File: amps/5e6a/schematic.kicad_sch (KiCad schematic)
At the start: 62 parts, among them T3 part not legible

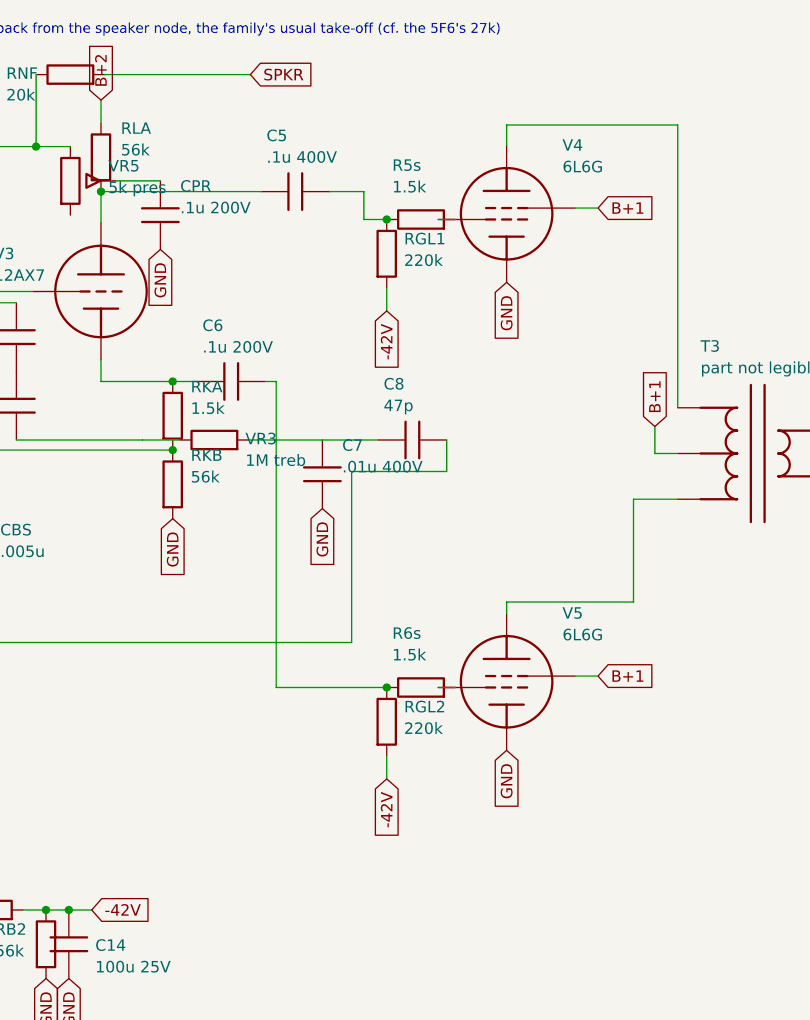
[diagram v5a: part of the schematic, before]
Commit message: Fix: schematic wiring on 5c1, 5e1, 5e4a, 5e5a, 5e6a, 5f4; all six claim equivalence
- 5c1, 5e1: the B+1/B+2/B+3 labels sat 3.56 mm above the filter chain with
  no lead, naming rails the drawing never reached
- 5e4a, 5e5a, 5e6a, 5f4: the 220k grid leak tapped the coupling-cap node;
  the netlist and the factory-derived layouts both return it at the grid
  pin after the 1.5k stopper (coupler -> stopper -> grid, as jtm45 draws
  it); each stopper now lands on the pentode's own grid pin and the leak
  hangs off that junction
- sch_map.yaml schematic_claim: verified on all six -> 37 of 38 sheets are
  hard-gated; 6g5 stays unclaimed (presence-branch DC path is a source
  question, not a declaration)

Co-Authored-By: Claude Fable 5.1 <noreply@anthropic.com>
Claude-Session: https://claude.ai/code/session_01KBMfdh37HmCL2iWcBiL5J1
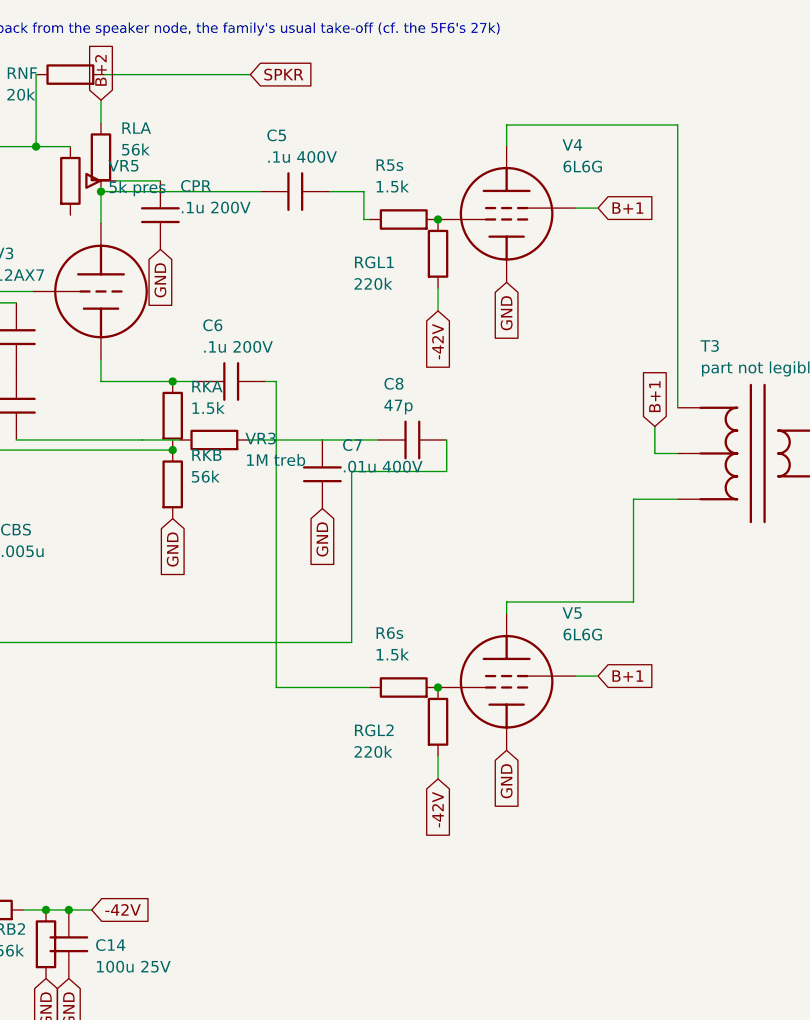
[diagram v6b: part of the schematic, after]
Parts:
- removed RB1: 3.3k, symbol cx:R
- removed RD2: 10k, symbol cx:R
- added C12: 16u, symbol cx:C
- added D1: SEL, symbol cx:DIODE_SS
- RB1: renamed from D1; value SEL -> 3.3k; symbol cx:DIODE_SS -> cx:R
- RD2: renamed from C12; value 16u -> 10k; symbol cx:C -> cx:R
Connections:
- net -42V: now also RB1.2
- net B+2: now also C12.1
- net B+3: now also RD2.2
- net GND: now also C12.2; no longer RD2.2
- net HT_B: now also D1.1 (A); no longer RB1.1 (A)
- net at R5s.2, V4.2 (G1): now also RGL1.1
- net at C5.2, R5s.1: no longer RGL1.1
- net at C6.2, R6s.1: no longer RGL2.1
- net at R6s.2, V5.2 (G1): now also RGL2.1
- new net: D1.2 (K), RB1.1
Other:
- moved on the sheet: R5s
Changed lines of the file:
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@@
   (wire (pts (xy 205.242 31.37) (xy 205.242 34.47))
     (stroke (width 0) (type default)))
-  (wire (pts (xy 205.242 34.47) (xy 207.782 34.47))
-    (stroke (width 0) (type default)))
-  (symbol (lib_id "cx:R") (at 211.592 34.47 90) (unit 1)
-    (in_bom yes) (on_board yes)
-    (property "Reference" "R5s" (at 208.392 28.47 270) (effects (font (size 1.27 1.27)) (justify left)))
-    (property "Value" "1.5k" (at 208.392 30.87 270) (effects (font (size 1.27 1.27)) (justify left))))
   (symbol (lib_id "cx:PENTODE") (at 221.102 33.835 0) (unit 1)
     (in_bom yes) (on_board yes)
     (property "Reference" "V4" (at 227.302 26.235 0) (effects (font (size 1.27 1.27)) (justify left)))
     (property "Value" "6L6G" (at 227.302 28.635 0) (effects (font (size 1.27 1.27)) (justify left))))
-  (wire (pts (xy 215.402 34.47) (xy 213.482 34.47))
+  (symbol (lib_id "cx:R") (at 209.672 34.47 90) (unit 1)
+    (in_bom yes) (on_board yes)
+    (property "Reference" "R5s" (at 206.472 28.47 270) (effects (font (size 1.27 1.27)) (justify left)))
+    (property "Value" "1.5k" (at 206.472 30.87 270) (effects (font (size 1.27 1.27)) (justify left))))
+  (wire (pts (xy 205.242 34.47) (xy 205.862 34.47))
     (stroke (width 0) (type default)))
-  (junction (at 207.782 34.47) (diameter 0) (color 0 0 0 0))
-  (symbol (lib_id "cx:R") (at 207.782 38.28 0) (unit 1)
+  (junction (at 213.482 34.47) (diameter 0) (color 0 0 0 0))
+  (symbol (lib_id "cx:R") (at 213.482 38.28 0) (unit 1)
     (in_bom yes) (on_board yes)
-    (property "Reference" "RGL1" (at 209.698 36.64 0) (effects (font (size 1.27 1.27)) (justify left)))
-    (property "Value" "220k" (at 209.698 39.04 0) (effects (font (size 1.27 1.27)) (justify left))))
-  (wire (pts (xy 207.782 42.09) (xy 207.782 44.63))
+    (property "Reference" "RGL1" (at 204.082 39.28 0) (effects (font (size 1.27 1.27)) (justify left)))
+    (property "Value" "220k" (at 204.082 41.68 0) (effects (font (size 1.27 1.27)) (justify left))))
+  (wire (pts (xy 213.482 42.09) (xy 213.482 44.63))
     (stroke (width 0) (type default)))
-  (global_label "-42V" (shape input) (at 207.782 44.63 270)
+  (global_label "-42V" (shape input) (at 213.482 44.63 270)
     (effects (font (size 1.27 1.27)) (justify right)))
   (wire (pts (xy 228.722 33.2) (xy 231.262 33.2))
@@
   (wire (pts (xy 195.502 86.47) (xy 205.242 86.47))
     (stroke (width 0) (type default)))
-  (wire (pts (xy 205.242 86.47) (xy 207.782 86.47))
-    (stroke (width 0) (type default)))
-  (symbol (lib_id "cx:R") (at 211.592 86.47 90) (unit 1)
-    (in_bom yes) (on_board yes)
-    (property "Reference" "R6s" (at 208.392 80.47 270) (effects (font (size 1.27 1.27)) (justify left)))
-    (property "Value" "1.5k" (at 208.392 82.87 270) (effects (font (size 1.27 1.27)) (justify left))))
   (symbol (lib_id "cx:PENTODE") (at 221.102 85.835 0) (unit 1)
     (in_bom yes) (on_board yes)
     (property "Reference" "V5" (at 227.302 78.235 0) (effects (font (size 1.27 1.27)) (justify left)))
     (property "Value" "6L6G" (at 227.302 80.635 0) (effects (font (size 1.27 1.27)) (justify left))))
-  (wire (pts (xy 215.402 86.47) (xy 213.482 86.47))
+  (symbol (lib_id "cx:R") (at 209.672 86.47 90) (unit 1)
+    (in_bom yes) (on_board yes)
+    (property "Reference" "R6s" (at 206.472 80.47 270) (effects (font (size 1.27 1.27)) (justify left)))
+    (property "Value" "1.5k" (at 206.472 82.87 270) (effects (font (size 1.27 1.27)) (justify left))))
+  (wire (pts (xy 205.242 86.47) (xy 205.862 86.47))
     (stroke (width 0) (type default)))
-  (junction (at 207.782 86.47) (diameter 0) (color 0 0 0 0))
-  (symbol (lib_id "cx:R") (at 207.782 90.28 0) (unit 1)
+  (junction (at 213.482 86.47) (diameter 0) (color 0 0 0 0))
+  (symbol (lib_id "cx:R") (at 213.482 90.28 0) (unit 1)
     (in_bom yes) (on_board yes)
-    (property "Reference" "RGL2" (at 209.698 88.64 0) (effects (font (size 1.27 1.27)) (justify left)))
-    (property "Value" "220k" (at 209.698 91.04 0) (effects (font (size 1.27 1.27)) (justify left))))
-  (wire (pts (xy 207.782 94.09) (xy 207.782 96.63))
+    (property "Reference" "RGL2" (at 204.082 91.28 0) (effects (font (size 1.27 1.27)) (justify left)))
+    (property "Value" "220k" (at 204.082 93.68 0) (effects (font (size 1.27 1.27)) (justify left))))
+  (wire (pts (xy 213.482 94.09) (xy 213.482 96.63))
     (stroke (width 0) (type default)))
-  (global_label "-42V" (shape input) (at 207.782 96.63 270)
+  (global_label "-42V" (shape input) (at 213.482 96.63 270)
     (effects (font (size 1.27 1.27)) (justify right)))
   (wire (pts (xy 228.722 85.2) (xy 231.262 85.2))

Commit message: Add: real tube pin numbers and readable valve glyphs on every schematic
Phase B of the drawing program. A factory service sheet numbers every tube
pin, because the number is what a technician puts a probe on. This corpus
printed none, and the numbers hidden in its symbols were positional
placeholders (P=1, G=2, K=3) that would have published a 6V6GT's plate as
pin 1 when it is pin 3.

1055 electrodes now carry the real number, 1027 lettered (27 are shared
filaments deduped, 1 dropped for want of clear space on the 6G2). Resolved per
instance from reference/tubes/<slug>.yaml through the same alias resolution the
layout renderer uses, so a 12AX7 section and a 6SL7 section each get their own
basing. A valve whose basing the corpus does not carry prints nothing rather
than a wrong number.

Section letters and basing units are now separate things, which cost a detour
worth recording. The RCA 12AX7-A sheet reads "Pin 1 - Plate of Unit No.2 ...
Pin 6 - Plate of Unit No.1", so unit numbering is not pin order; the 5Y3 and
GZ34 number their units in opposite pin order, so nothing positional can
express it. But the section LETTER is a designator, not a basing fact: this
corpus, like every technician, calls the first stage in signal order V1A, and
five amps' prose already did. On four amps the factory sheets put that first
stage on the other half -- the AA764's own schematic prints +200 V on pin 1 --
so those drawings now state their unit explicitly, each citing its source, and
no letter, netlist, parts list or layout comment changed. 183 layout comments
agree with the printed numbers, 0 disagree. A guard fires if two halves of one
bottle resolve to the same unit, which is exactly how this was found.

Glyphs: the cathode gains a bracket and filament hairpin so it can no longer be
confused with the plate bar, the pentode's screen sits on its own row, and a
rectifier draws as one envelope over its sections instead of two apparent
bottles. Line weights are scaled per sheet to a co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
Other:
- note added: "1"
- note added: "2"
- note added: "2,8"
- note added: "3"
- note added: "4"
- note added: "5"
- note added: "6"
- note added: "7"
- note added: "8"

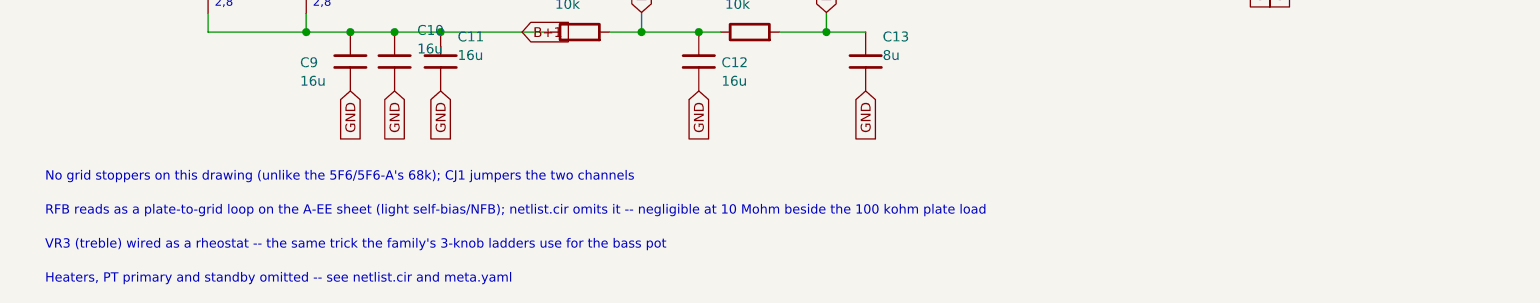
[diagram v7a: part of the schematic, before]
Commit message: Fix: schematic sheet notes no longer name repository files
Thirty-seven committed sheets rendered footnotes and section notes such as
"Heaters and PT primary omitted — see netlist.cir and meta.yaml" or
"excluded from netlist.cir (notes.md)" to visitors through KiCanvas. The
prose sweeps never counted sheets. Rewritten in the site's own words — the
netlist, the sources list, the circuit story, the parts list, the board
drawing — in 59 strings across 33 draw scripts, keeping every technical
claim as it was; the three tone sheets (6G4, 6G5, 6G6-B) are under repair
elsewhere and keep theirs for now. The sweep touched only strings passed to
the sheet's note, text, caption and footnote calls, never a path or a value.

Gates: check_schematics 40/0, connectivity 0 isolated pins;
verify_schematic_nets 40 clean; only the regenerated sheets and their served
copies changed.

Co-Authored-By: Claude Fable 5.1 <noreply@anthropic.com>
Claude-Session: https://claude.ai/code/session_01KBMfdh37HmCL2iWcBiL5J1
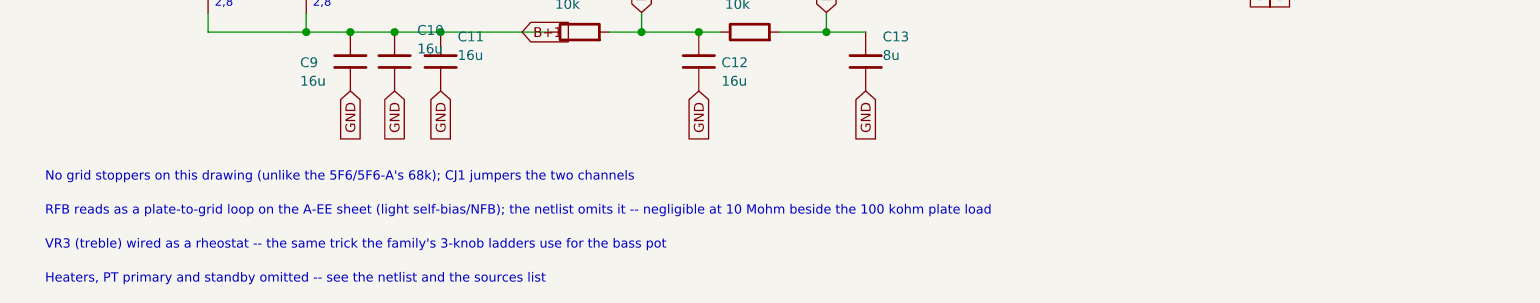
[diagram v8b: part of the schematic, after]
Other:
- note added: "Heaters, PT primary and standby omitted -- see the netlist and the sources list"
- note added: "RFB reads as a plate-to-grid loop on the A-EE sheet (light self-bias/NFB); the netlist omits it -- negligible at 10 Mohm beside the 100 kohm plate load"
- note removed: "Heaters, PT primary and standby omitted -- see netlist.cir and meta.yaml"
- note removed: "RFB reads as a plate-to-grid loop on the A-EE sheet (light self-bias/NFB); netlist.cir omits it -- negligible at 10 Mohm beside the 100 kohm plate load"
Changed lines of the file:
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@@
   (text "No grid stoppers on this drawing (unlike the 5F6/5F6-A's 68k); CJ1 jumpers the two channels" (at 12.7 147.048 0)
     (effects (font (size 1.2 1.2)) (justify left)))
-  (text "RFB reads as a plate-to-grid loop on the A-EE sheet (light self-bias/NFB); netlist.cir omits it -- negligible at 10 Mohm beside the 100 kohm plate load" (at 12.7 151.448 0)
+  (text "RFB reads as a plate-to-grid loop on the A-EE sheet (light self-bias/NFB); the netlist omits it -- negligible at 10 Mohm beside the 100 kohm plate load" (at 12.7 151.448 0)
     (effects (font (size 1.2 1.2)) (justify left)))
   (text "VR3 (treble) wired as a rheostat -- the same trick the family's 3-knob ladders use for the bass pot" (at 12.7 155.848 0)
     (effects (font (size 1.2 1.2)) (justify left)))
-  (text "Heaters, PT primary and standby omitted -- see netlist.cir and meta.yaml" (at 12.7 160.248 0)
+  (text "Heaters, PT primary and standby omitted -- see the netlist and the sources list" (at 12.7 160.248 0)
     (effects (font (size 1.2 1.2)) (justify left)))
   (sheet_instances (path "/" (page "1")))
